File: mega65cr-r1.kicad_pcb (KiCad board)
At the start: 2 copper layers, 22 parts, among them J13 Conn_01x04_Male, J14 Conn_02x17_Odd_Even, J16 Conn_01x04_Male, J6 SDF-60J for IEC 1541 serial p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, U1 74HC245, U2 74HC245, U22 74LS06N, U3 74HC245

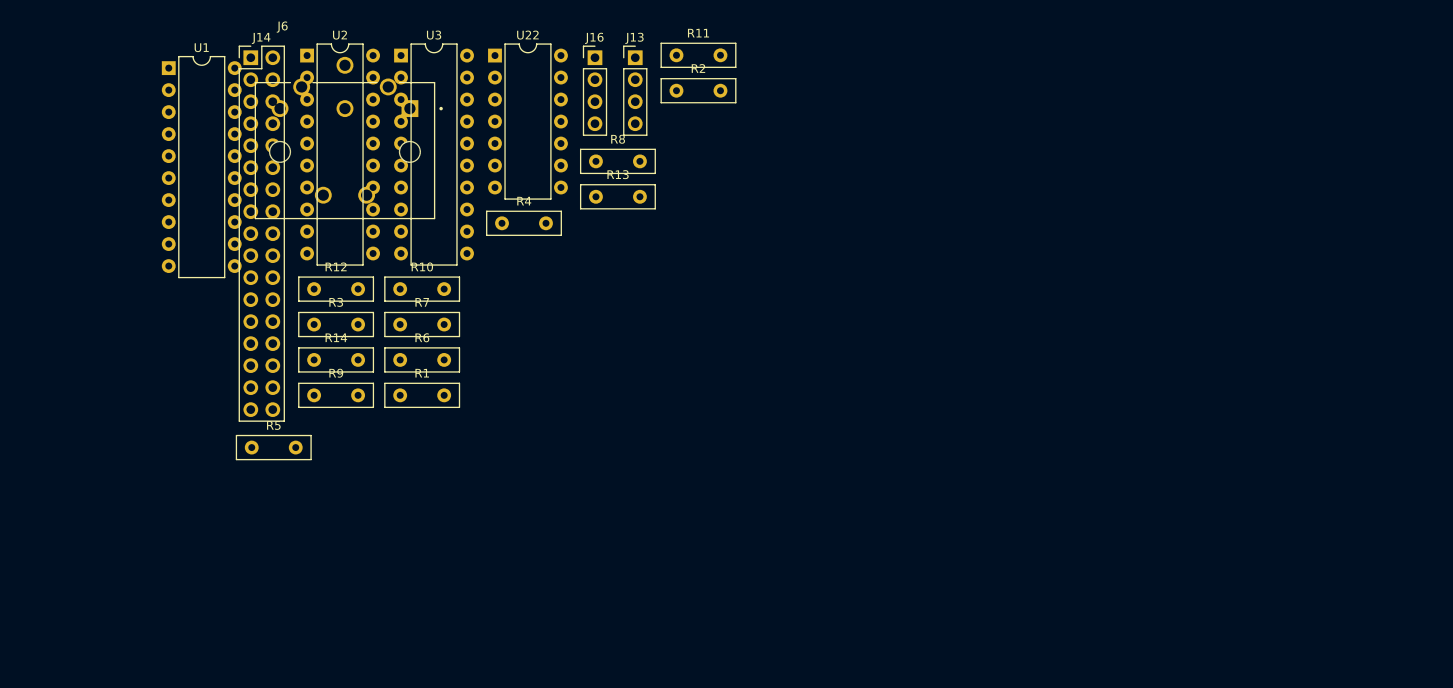
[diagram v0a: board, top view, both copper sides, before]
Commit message: add all missing footprints
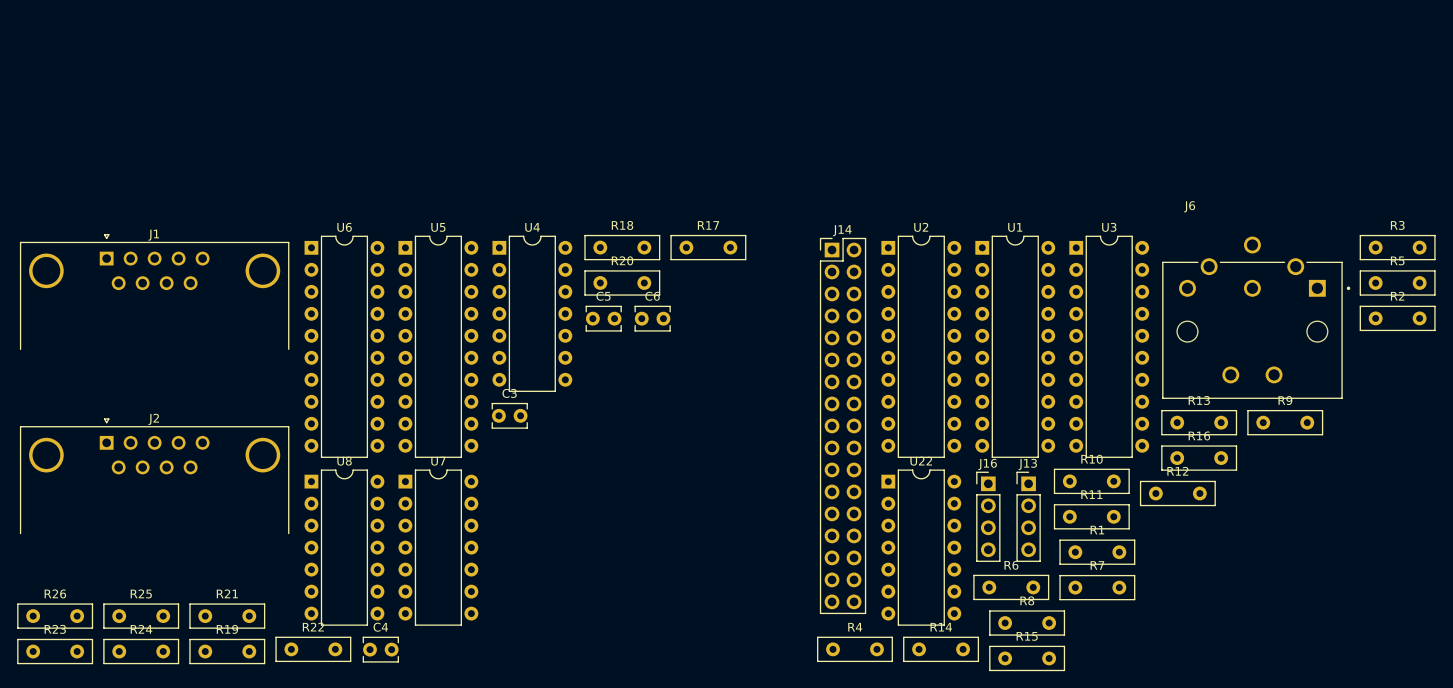
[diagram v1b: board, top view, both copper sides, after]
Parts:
- added C3: 1.2nF, Capacitor_THT:C_Disc_D3.8mm_W2.6mm_P2.50mm, F.Cu at (167.6, 124.5)
- added C4: 1.2nF, Capacitor_THT:C_Disc_D3.8mm_W2.6mm_P2.50mm, F.Cu at (152.8, 151.5)
- added C5: 1.2nF, Capacitor_THT:C_Disc_D3.8mm_W2.6mm_P2.50mm, F.Cu at (178.5, 113.2)
- added C6: 1.2nF, Capacitor_THT:C_Disc_D3.8mm_W2.6mm_P2.50mm, F.Cu at (184.1, 113.2)
- added J1: DB9_Male_MountingHoles, Connector_Dsub:DSUB-9_Male_Horizontal_P2.77x2.84mm_EdgePinOffset7.70mm_Housed_MountingHolesOffset9.12mm, F.Cu at (122.3, 106.3)
- added J2: DB9_Male_MountingHoles, Connector_Dsub:DSUB-9_Male_Horizontal_P2.77x2.84mm_EdgePinOffset7.70mm_Housed_MountingHolesOffset9.12mm, F.Cu at (122.3, 127.6)
- added R15: 4K7, Resistor_THT:R_Box_L8.4mm_W2.5mm_P5.08mm, F.Cu at (226.1, 152.5)
- added R16: 4K7, Resistor_THT:R_Box_L8.4mm_W2.5mm_P5.08mm, F.Cu at (246.0, 129.3)
- added R17: 4K7, Resistor_THT:R_Box_L8.4mm_W2.5mm_P5.08mm, F.Cu at (189.3, 105.0)
- added R18: 4K7, Resistor_THT:R_Box_L8.4mm_W2.5mm_P5.08mm, F.Cu at (179.3, 105.0)
- added R19: 4K7, Resistor_THT:R_Box_L8.4mm_W2.5mm_P5.08mm, F.Cu at (133.7, 151.7)
- added R20: 4K7, Resistor_THT:R_Box_L8.4mm_W2.5mm_P5.08mm, F.Cu at (179.3, 109.1)
- added R21: 4K7, Resistor_THT:R_Box_L8.4mm_W2.5mm_P5.08mm, F.Cu at (133.7, 147.6)
- added R22: 4K7, Resistor_THT:R_Box_L8.4mm_W2.5mm_P5.08mm, F.Cu at (143.7, 151.4)
- added R23: 4K7, Resistor_THT:R_Box_L8.4mm_W2.5mm_P5.08mm, F.Cu at (113.8, 151.7)
- added R24: 4K7, Resistor_THT:R_Box_L8.4mm_W2.5mm_P5.08mm, F.Cu at (123.8, 151.7)
- added R25: 4K7, Resistor_THT:R_Box_L8.4mm_W2.5mm_P5.08mm, F.Cu at (123.8, 147.6)
- added R26: 4K7, Resistor_THT:R_Box_L8.4mm_W2.5mm_P5.08mm, F.Cu at (113.8, 147.6)
- added U4: 74LS06N, Package_DIP:DIP-14_W7.62mm, F.Cu at (167.7, 105.1)
- added U5: 74HC245, Package_DIP:DIP-20_W7.62mm, F.Cu at (156.8, 105.1)
- added U6: 74HC245, Package_DIP:DIP-20_W7.62mm, F.Cu at (146.0, 105.1)
- added U7: 74LS06N, Package_DIP:DIP-14_W7.62mm, F.Cu at (156.8, 132.1)
- added U8: 74LS06N, Package_DIP:DIP-14_W7.62mm, F.Cu at (146.0, 132.1)
- R1, R2, R3, R4, R5: value 4K7 -> 1K
- R11, R12, R13: value 1K -> 4K7
- moved R5 131.2 mm to (268.9, 109.1)
- moved R3 122.9 mm to (268.9, 105.0)
- moved R9 109.7 mm to (255.9, 125.2)
- moved J6 106.8 mm to (254.7, 114.7)
- moved R12 100.0 mm to (243.5, 133.4)
- moved U1 96.2 mm to (223.5, 105.1)
- moved R2 84.9 mm to (268.9, 113.2)
- moved R7 83.7 mm to (234.2, 144.3)
- moved U3 81.1 mm to (234.3, 105.1)
- moved R10 80.5 mm to (233.6, 132.0)
- moved R1 80.1 mm to (234.2, 140.2)
- moved R14 77.4 mm to (216.2, 151.4)
- moved R6 72.9 mm to (224.3, 144.3)
- moved R13 72.0 mm to (246.0, 125.2)
- moved R8 71.2 mm to (226.1, 148.4)
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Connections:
- net /DIR renamed /Floppy Interfaces/DIR
- net /DRVSA renamed /Floppy Interfaces/DRVSA
- net /MOTEA renamed /Floppy Interfaces/MOTEA
- net /MOTEB renamed /Floppy Interfaces/MOTEB
- net /REDWC renamed /Floppy Interfaces/REDWC
- net /SIDE1 renamed /Floppy Interfaces/SIDE1
- net /STEP renamed /Floppy Interfaces/STEP
- net /WDATA renamed /Floppy Interfaces/WDATA
- net /WGATE renamed /Floppy Interfaces/WGATE
- J14 pad 12: /DRVSB -> /Floppy Interfaces/DRVSB
- J14 pad 26: /TRCK0 -> /Floppy Interfaces/TRCK0
- J14 pad 28: /WPROT -> /Floppy Interfaces/WPROT
- J14 pad 30: /RDATA -> /Floppy Interfaces/RDATA
- J14 pad 34: /DISKCHG -> /Floppy Interfaces/DISKCHG
- J14 pad 8: /INDEX -> /Floppy Interfaces/INDEX
- J6 pad 1: /SER_SRQ -> /Floppy Interfaces/SER_SRQ
- J6 pad 3: /SER_ATN -> /Floppy Interfaces/SER_ATN
- J6 pad 4: /SER_CLK -> /Floppy Interfaces/SER_CLK
- J6 pad 5: /SER_DATA -> /Floppy Interfaces/SER_DATA
- J6 pad 6: /SER_RESET -> /Floppy Interfaces/SER_RESET
- R1 pad 1: unconnected-(R1-Pad1) -> Net-(U2-Pad18)
- R1 pad 2: /INDEX -> /Floppy Interfaces/SER_RESET
- R10 pad 1: Net-(R10-Pad1) -> Net-(U3-Pad14)
- R10 pad 2: /DISKCHG -> /Floppy Interfaces/DISKCHG
- R11 pad 1: Net-(R11-Pad1) -> /Floppy Interfaces/DRVSB
- R11 pad 2: /SER_CLK -> +5V
- R12 pad 1: Net-(R12-Pad1) -> unconnected-(R12-Pad1)
- R12 pad 2: /SER_DATA -> /Floppy Interfaces/INDEX
- R13 pad 1: Net-(R13-Pad1) -> /Floppy Interfaces/TRCK0
- R13 pad 2: /SER_ATN -> unconnected-(R13-Pad2)
- R14 pad 1: /DRVSB -> /Floppy Interfaces/WPROT
- R14 pad 2: +5V -> unconnected-(R14-Pad2)
- R2 pad 1: /TRCK0 -> Net-(U2-Pad17)
- R2 pad 2: unconnected-(R2-Pad2) -> /Floppy Interfaces/SER_SRQ
- R3 pad 1: /WPROT -> Net-(U2-Pad16)
- R3 pad 2: unconnected-(R3-Pad2) -> /Floppy Interfaces/SER_CLK
- R4 pad 1: /RDATA -> Net-(U2-Pad15)
- R4 pad 2: unconnected-(R4-Pad2) -> /Floppy Interfaces/SER_DATA
- R5 pad 1: /DISKCHG -> Net-(U2-Pad14)
- R5 pad 2: unconnected-(R5-Pad2) -> /Floppy Interfaces/SER_ATN
- R6 pad 1: Net-(R6-Pad1) -> Net-(U3-Pad18)
- R6 pad 2: /INDEX -> /Floppy Interfaces/INDEX
- R7 pad 1: Net-(R7-Pad1) -> Net-(U3-Pad17)
- R7 pad 2: /TRCK0 -> /Floppy Interfaces/TRCK0
- R8 pad 1: Net-(R8-Pad1) -> Net-(U3-Pad16)
- R8 pad 2: /WPROT -> /Floppy Interfaces/WPROT
- R9 pad 1: Net-(R9-Pad1) -> Net-(U3-Pad15)
- R9 pad 2: /RDATA -> /Floppy Interfaces/RDATA
- U2 pad 11: Net-(R13-Pad1) -> unconnected-(U2-Pad11)
- U2 pad 12: Net-(R12-Pad1) -> unconnected-(U2-Pad12)
- U2 pad 13: Net-(R11-Pad1) -> unconnected-(U2-Pad13)
- U2 pad 14: Net-(R10-Pad1) -> Net-(U2-Pad14)
- U2 pad 15: Net-(R9-Pad1) -> Net-(U2-Pad15)
- U2 pad 16: Net-(R8-Pad1) -> Net-(U2-Pad16)
- U2 pad 17: Net-(R7-Pad1) -> Net-(U2-Pad17)
- U2 pad 18: Net-(R6-Pad1) -> Net-(U2-Pad18)
- U2 pad 2: F_INDEX -> F_SER_RESET_IN
- U2 pad 3: F_TRCK0 -> F_SER_SRQ_IN
- U2 pad 4: F_WPROT -> F_SER_CLK_IN
- U2 pad 5: F_RDATA -> F_SER_RESET_IN
- U2 pad 6: F_DISKCHG -> F_SER_ATN_IN
- U2 pad 7: F_SER_CLK_IN -> unconnected-(U2-Pad7)
- U2 pad 8: F_SER_RESET_IN -> unconnected-(U2-Pad8)
- U2 pad 9: F_SER_ATN_IN -> unconnected-(U2-Pad9)
- U22 pad 10: /SER_SRQ -> /Floppy Interfaces/SER_SRQ
- U22 pad 12: /SER_DATA -> /Floppy Interfaces/SER_DATA
- U22 pad 2: /DRVSB -> /Floppy Interfaces/DRVSB
- U22 pad 4: /SER_CLK -> /Floppy Interfaces/SER_CLK
- U22 pad 6: /SER_RESET -> /Floppy Interfaces/SER_RESET
- U22 pad 8: /SER_ATN -> /Floppy Interfaces/SER_ATN
- U3 pad 1: unconnected-(U3-Pad1) -> GND
- U3 pad 10: unconnected-(U3-Pad10) -> GND
- U3 pad 14: unconnected-(U3-Pad14) -> Net-(U3-Pad14)
- U3 pad 15: unconnected-(U3-Pad15) -> Net-(U3-Pad15)
- U3 pad 16: unconnected-(U3-Pad16) -> Net-(U3-Pad16)
- U3 pad 17: unconnected-(U3-Pad17) -> Net-(U3-Pad17)
- U3 pad 18: unconnected-(U3-Pad18) -> Net-(U3-Pad18)
- U3 pad 19: unconnected-(U3-Pad19) -> GND
- U3 pad 2: unconnected-(U3-Pad2) -> F_INDEX
- U3 pad 20: unconnected-(U3-Pad20) -> +3V3
- U3 pad 3: unconnected-(U3-Pad3) -> F_TRCK0
- U3 pad 4: unconnected-(U3-Pad4) -> F_WPROT
- U3 pad 5: unconnected-(U3-Pad5) -> F_RDATA
- U3 pad 6: unconnected-(U3-Pad6) -> F_DISKCHG

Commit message: add mezannine for joystick ports to de-clutter board.
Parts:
- added C1: 0.1uF, Capacitor_THT:C_Disc_D6.0mm_W4.4mm_P5.00mm, F.Cu at (116.8, 363.2)
- added C10: 0.1uF, Capacitor_THT:C_Disc_D6.0mm_W4.4mm_P5.00mm, F.Cu at (154.2, 333.3)
- added C11: 0.1uF, Capacitor_THT:C_Disc_D6.0mm_W4.4mm_P5.00mm, F.Cu at (131.1, 348.6)
- added C12: 15uF 50V, Capacitor_THT:CP_Radial_D5.0mm_P2.00mm, F.Cu at (351.0, 236.7)
- added C13: 15uF 50V, Capacitor_THT:CP_Radial_D5.0mm_P2.00mm, F.Cu at (382.5, 209.3)
- added C14: 15uF 50V, Capacitor_THT:CP_Radial_D5.0mm_P2.00mm, F.Cu at (339.2, 250.1)
- added C15: 0.47uF eg FG28X7R1H474KRT0, Capacitor_THT:C_Disc_D6.0mm_W4.4mm_P5.00mm, F.Cu at (368.6, 214.7)
- added C16: 100nF 50V, Capacitor_THT:C_Disc_D6.0mm_W4.4mm_P5.00mm, F.Cu at (381.7, 203.0)
- added C17: 180uF 16V, Capacitor_THT:CP_Radial_D10.0mm_P5.00mm, F.Cu at (340.4, 241.1)
- added C18: 180uF 16V, Capacitor_THT:CP_Radial_D10.0mm_P5.00mm, F.Cu at (351.9, 227.6)
- added C2: 0.01uF, eg K103Z15Y5VE5TH5, Capacitor_THT:C_Disc_D6.0mm_W4.4mm_P5.00mm, F.Cu at (125.0, 363.2)
- added C7: 0.1uF, Capacitor_THT:C_Disc_D6.0mm_W4.4mm_P5.00mm, F.Cu at (177.8, 309.8)
- added C8: 1uF, Capacitor_THT:C_Disc_D6.0mm_W4.4mm_P5.00mm, F.Cu at (131.1, 354.5)
- added C9: 10uF, Capacitor_THT:C_Disc_D6.0mm_W4.4mm_P5.00mm, F.Cu at (139.3, 347.2)
- added D1: 5V 40V 1N5825, Diode_THT:D_5KP_P12.70mm_Horizontal, F.Cu at (339.0, 216.3)
- added FB1: FerriteBead FT-3AMB4ARLY-PF, snapeda:Ferrite_Bead_Axial_L10.0mm_D4.5mm_P15.00mm_Horizontal, F.Cu at (50.9, 307.5)
- added J10: Molex 46765-2301, Connector_HDMI:HDMI_A_Contact_Technology_HDMI-19APL2_Horizontal, F.Cu at (193.0, 33.0)
- added J11: CON-SOCJ-2155, snapeda:GRAVITECH_CON-SOCJ-2155, F.Cu at (40.6, 38.1)
- added J12: Header for power lead to QMTECH WUKONG FPGA board, Connector_PinHeader_2.54mm:PinHeader_1x02_P2.54mm_Vertical, F.Cu at (362.5, 219.2)
- added J15: 696101000002 Fuse Holder 20mm, snapeda:696101000002, F.Cu at (63.5, 88.9)
- added J17: C64_Tape_Port, HackupNet:C64-Cassette-Port-Male, F.Cu at (446.5, 41.5)
- added J18: BA60BC0WT, snapeda:TO-220-FP-5, F.Cu at (138.0, 221.7)
- added J19: C64_User_Port, snapeda:C64-User-Port-Male, F.Cu at (298.3, 41.5)
- added J20: C64_Expansion_Port, HackupNet:C64-Cart-Socket-Vertical, F.Cu at (85.0, 66.0)
- added J21: Audio Header, Connector_PinHeader_2.54mm:PinHeader_1x05_P2.54mm_Vertical, F.Cu at (259.1, 245.6)
- added J22: DB15_Female_HighDensity_MountingHoles, Connector_Dsub:DSUB-15-HD_Female_Horizontal_P2.29x1.98mm_EdgePinOffset8.35mm_Housed_MountingHolesOffset10.89mm, F.Cu at (158.3, 51.5)
- added J23: 3.5mm_Stereo_Audio_Jack STX-3500-4N, Connector_Audio:Jack_3.5mm_CUI_SJ-3524-SMT_Horizontal, F.Cu at (251.5, 38.1)
- added J24: Component A/V, snapeda:CUI_SDF-80J, F.Cu at (345.4, 38.1)
- added J25: Joystick Ports Mezannine Lower, Connector_PinHeader_2.54mm:PinHeader_2x20_P2.54mm_Vertical, F.Cu at (64.8, 151.1)
- added J26: Joystick Ports Mezannine Upper, Connector_PinHeader_2.54mm:PinHeader_2x20_P2.54mm_Vertical, F.Cu at (-29.2, 163.8)
- added J3: Wuerth_7499010121A, Connector_RJ:RJ45_Wuerth_7499010121A_Horizontal, F.Cu at (210.8, 48.3)
- added J4: QMTECH FPGA Module U4, Connector_PinHeader_2.54mm:PinHeader_2x32_P2.54mm_Vertical, F.Cu at (268.0, 72.4)
- added J5: QMTECH FPGA Module U5, Connector_PinHeader_2.54mm:PinHeader_2x32_P2.54mm_Vertical, F.Cu at (268.0, 151.1)
- added J7: QMTECH JTAG, Connector_PinSocket_2.54mm:PinSocket_1x06_P2.54mm_Vertical, F.Cu at (175.2, 287.8)
- added J8: RTC, Connector_PinHeader_2.54mm:PinHeader_1x05_P2.54mm_Vertical, F.Cu at (179.8, 287.8)
- added J9: 1140084168 microSD Card Slot, snapeda:AMPHENOL_1140084168, F.Cu at (236.2, 42.2)
- added JB1: TE0790-03, Connector_PinHeader_2.54mm:PinHeader_2x06_P2.54mm_Vertical, F.Cu at (168.0, 287.8)
- added L1: 22uH, eg SC30R22KT, Inductor_THT:L_Axial_L5.0mm_D3.6mm_P10.00mm_Horizontal_Murata_BL01RN1A2A2, F.Cu at (355.5, 214.3)
- added P1: Full-side CD Card Slot, snapeda:YAMAICHI_FPS009-2405-0, F.Cu at (162.6, 154.1)
- added R11: 4K7, Resistor_THT:R_Box_L8.4mm_W2.5mm_P5.08mm, F.Cu at (38.1, 182.9)
- added R27: 220, Resistor_THT:R_Axial_DIN0204_L3.6mm_D1.6mm_P7.62mm_Horizontal, F.Cu at (167.2, 304.4)
- added R28: 220, Resistor_THT:R_Axial_DIN0204_L3.6mm_D1.6mm_P7.62mm_Horizontal, F.Cu at (183.6, 287.0)
- added R29: 6.49K 1%, Resistor_THT:R_Axial_DIN0204_L3.6mm_D1.6mm_P7.62mm_Horizontal, F.Cu at (167.2, 307.5)
- added R30: 4K7, Resistor_THT:R_Box_L8.4mm_W2.5mm_P5.08mm, F.Cu at (168.1, 314.5)
- added R31: 4K7, Resistor_THT:R_Box_L8.4mm_W2.5mm_P5.08mm, F.Cu at (184.6, 294.8)
- added R32: 4K7, Resistor_THT:R_Box_L8.4mm_W2.5mm_P5.08mm, F.Cu at (155.1, 328.3)
- added R33: 4K7, Resistor_THT:R_Box_L8.4mm_W2.5mm_P5.08mm, F.Cu at (184.6, 298.8)
- added R34: 4K7, Resistor_THT:R_Box_L8.4mm_W2.5mm_P5.08mm, F.Cu at (178.7, 304.8)
- added R35: 4K7, Resistor_THT:R_Box_L8.4mm_W2.5mm_P5.08mm, F.Cu at (145.1, 332.4)
- added R36: 12K4, Resistor_THT:R_Box_L8.4mm_W2.5mm_P5.08mm, F.Cu at (145.1, 328.3)
- added R37: 4K7, Resistor_THT:R_Box_L8.4mm_W2.5mm_P5.08mm, F.Cu at (184.6, 290.7)
- added R38: 510R, Resistor_THT:R_Box_L8.4mm_W2.5mm_P5.08mm, F.Cu at (304.4, 202.1)
- added R39: 1K0, Resistor_THT:R_Box_L8.4mm_W2.5mm_P5.08mm, F.Cu at (324.3, 210.3)
- added R40: 2K0, Resistor_THT:R_Box_L8.4mm_W2.5mm_P5.08mm, F.Cu at (302.0, 231.9)
- added R41: 4K0, Resistor_THT:R_Box_L8.4mm_W2.5mm_P5.08mm, F.Cu at (259.2, 272.3)
- added R42: 8K0, Resistor_THT:R_Box_L8.4mm_W2.5mm_P5.08mm, F.Cu at (314.3, 210.3)
- added R43: 16K0, Resistor_THT:R_Box_L8.4mm_W2.5mm_P5.08mm, F.Cu at (302.0, 227.8)
- added R44: 510R, Resistor_THT:R_Box_L8.4mm_W2.5mm_P5.08mm, F.Cu at (314.3, 218.5)
- added R45: 1K0, Resistor_THT:R_Box_L8.4mm_W2.5mm_P5.08mm, F.Cu at (314.3, 206.2)
- added R46: 2K0, Resistor_THT:R_Box_L8.4mm_W2.5mm_P5.08mm, F.Cu at (269.1, 265.7)
- added R47: 4K0, Resistor_THT:R_Box_L8.4mm_W2.5mm_P5.08mm, F.Cu at (304.4, 218.5)
- added R48: 8K0, Resistor_THT:R_Box_L8.4mm_W2.5mm_P5.08mm, F.Cu at (269.1, 257.5)
- added R49: 16K0, Resistor_THT:R_Box_L8.4mm_W2.5mm_P5.08mm, F.Cu at (324.3, 202.1)
- added R50: 510R, Resistor_THT:R_Box_L8.4mm_W2.5mm_P5.08mm, F.Cu at (263.9, 253.4)
- added R51: 1K0, Resistor_THT:R_Box_L8.4mm_W2.5mm_P5.08mm, F.Cu at (273.8, 253.4)
- added R52: 2K0, Resistor_THT:R_Box_L8.4mm_W2.5mm_P5.08mm, F.Cu at (259.2, 268.2)
- added R53: 4K0, Resistor_THT:R_Box_L8.4mm_W2.5mm_P5.08mm, F.Cu at (293.7, 240.1)
- added R54: 8K0, Resistor_THT:R_Box_L8.4mm_W2.5mm_P5.08mm, F.Cu at (302.1, 223.8)
- added R55: 16K0, Resistor_THT:R_Box_L8.4mm_W2.5mm_P5.08mm, F.Cu at (282.1, 229.1)
- added R56: 510R, Resistor_THT:R_Box_L8.4mm_W2.5mm_P5.08mm, F.Cu at (259.2, 264.2)
- added R57: 1K0, Resistor_THT:R_Box_L8.4mm_W2.5mm_P5.08mm, F.Cu at (259.2, 260.1)
- added R58: 2K0, Resistor_THT:R_Box_L8.4mm_W2.5mm_P5.08mm, F.Cu at (314.3, 202.1)
- added R59: 4K0, Resistor_THT:R_Box_L8.4mm_W2.5mm_P5.08mm, F.Cu at (292.1, 231.9)
- added R60: 8K0, Resistor_THT:R_Box_L8.4mm_W2.5mm_P5.08mm, F.Cu at (292.1, 236.0)
- added R61: 16K0, Resistor_THT:R_Box_L8.4mm_W2.5mm_P5.08mm, F.Cu at (304.4, 214.4)
- added R62: 510R, Resistor_THT:R_Box_L8.4mm_W2.5mm_P5.08mm, F.Cu at (312.0, 222.6)
- added R63: 1K0, Resistor_THT:R_Box_L8.4mm_W2.5mm_P5.08mm, F.Cu at (282.1, 225.0)
- added R64: 2K0, Resistor_THT:R_Box_L8.4mm_W2.5mm_P5.08mm, F.Cu at (263.9, 245.3)
- added R65: 4K0, Resistor_THT:R_Box_L8.4mm_W2.5mm_P5.08mm, F.Cu at (324.3, 206.2)
- added R66: 8K0, Resistor_THT:R_Box_L8.4mm_W2.5mm_P5.08mm, F.Cu at (304.4, 210.3)
- added R67: 16K0, Resistor_THT:R_Box_L8.4mm_W2.5mm_P5.08mm, F.Cu at (282.1, 237.2)
- added R68: 510R, Resistor_THT:R_Box_L8.4mm_W2.5mm_P5.08mm, F.Cu at (292.1, 227.8)
- added R69: 1K0, Resistor_THT:R_Box_L8.4mm_W2.5mm_P5.08mm, F.Cu at (269.1, 261.6)
- added R70: 2K0, Resistor_THT:R_Box_L8.4mm_W2.5mm_P5.08mm, F.Cu at (283.7, 241.3)
- added R71: 4K0, Resistor_THT:R_Box_L8.4mm_W2.5mm_P5.08mm, F.Cu at (292.1, 223.8)
- added R72: 8K0, Resistor_THT:R_Box_L8.4mm_W2.5mm_P5.08mm, F.Cu at (304.4, 206.2)
- added R73: 16K0, Resistor_THT:R_Box_L8.4mm_W2.5mm_P5.08mm, F.Cu at (314.3, 214.4)
- added R74: 510R, Resistor_THT:R_Box_L8.4mm_W2.5mm_P5.08mm, F.Cu at (283.7, 245.4)
- added R75: 1K0, Resistor_THT:R_Box_L8.4mm_W2.5mm_P5.08mm, F.Cu at (263.9, 249.4)
- added R76: 2K0, Resistor_THT:R_Box_L8.4mm_W2.5mm_P5.08mm, F.Cu at (273.8, 245.3)
- added R77: 4K0, Resistor_THT:R_Box_L8.4mm_W2.5mm_P5.08mm, F.Cu at (273.8, 249.4)
- added R78: 8K0, Resistor_THT:R_Box_L8.4mm_W2.5mm_P5.08mm, F.Cu at (283.7, 249.5)
- added R79: 16K0, Resistor_THT:R_Box_L8.4mm_W2.5mm_P5.08mm, F.Cu at (279.1, 257.5)
- added R80: 49R9, Resistor_THT:R_Box_L8.4mm_W2.5mm_P5.08mm, F.Cu at (259.2, 276.4)
- added R81: 49R9, Resistor_THT:R_Box_L8.4mm_W2.5mm_P5.08mm, F.Cu at (282.1, 233.2)
- added RN1: 3.3K x 8, Resistor_THT:R_Array_SIP9, F.Cu at (68.6, 297.2)
- added RN2: 4609X-AP1-332LF 3.3Kx8, Resistor_THT:R_Array_SIP9, F.Cu at (190.7, 269.3)
- added RN3: 3.3K x 8, Resistor_THT:R_Array_SIP9, F.Cu at (190.7, 256.2)
- added RN4: 3.3K x 8, Resistor_THT:R_Array_SIP9, F.Cu at (190.7, 260.6)
- added RN5: 3.3K x 8, Resistor_THT:R_Array_SIP9, F.Cu at (158.1, 279.9)
- added RN6: 3.3K x 8, Resistor_THT:R_Array_SIP9, F.Cu at (190.7, 264.9)
- added S1: 418117270908, snapeda:418117270908, F.Cu at (78.7, 307.3)
- added SW1: SW_Push_DPDT, snapeda:SPUJ191500, F.Cu at (17.8, 175.3)
- added U1: 74LS373, Package_DIP:DIP-20_W7.62mm, F.Cu at (257.6, 341.5)
- added U10: 74LS06N, Package_DIP:DIP-14_W7.62mm, F.Cu at (-118.1, 223.5)
- added U11: 74LS06N, Package_DIP:DIP-14_W7.62mm, F.Cu at (-41.9, 226.1)
- added U12: DP83826, Package_DFN_QFN:QFN-32-1EP_5x5mm_P0.5mm_EP3.3x3.3mm_ThermalVias, F.Cu at (210.3, 61.5)
- added U13: 74LVC374, Package_DIP:DIP-20_W7.62mm, F.Cu at (54.6, 280.7)
- added U14: PTN3363BSMP, snapeda:QFN50P500X500X85-33N, F.Cu at (193.0, 45.7)
- added U15: LM2678T-5.0, snapeda:TO127P457X1016X2052-7P, F.Cu at (346.4, 222.6)
- added U16: 74LVC374, Package_DIP:DIP-20_W7.62mm, F.Cu at (52.8, 229.0)
- added U17: 74LVC374, Package_DIP:DIP-20_W7.62mm, F.Cu at (115.6, 202.1)
- added U18: 74LS373, Package_DIP:DIP-20_W7.62mm, F.Cu at (81.1, 215.6)
- added U19: 74LS373, Package_DIP:DIP-20_W7.62mm, F.Cu at (104.7, 202.1)
- added U2: 74LVC374, Package_DIP:DIP-20_W7.62mm, F.Cu at (268.5, 287.5)
- added U20: 74LS125, Package_DIP:DIP-14_W7.62mm, F.Cu at (113.7, 229.1)
- added U21: 74LS125, Package_DIP:DIP-14_W7.62mm, F.Cu at (102.8, 229.1)
- added U23: 74LVC374, Package_DIP:DIP-20_W7.62mm, F.Cu at (126.4, 202.1)
- added U24: 74LS125, Package_DIP:DIP-14_W7.62mm, F.Cu at (124.5, 229.1)
- added U25: 74LS373, Package_DIP:DIP-20_W7.62mm, F.Cu at (63.6, 229.0)
- added U26: 74LS373, Package_DIP:DIP-20_W7.62mm, F.Cu at (92.0, 229.1)
- added U27: 74LS138, Package_DIP:DIP-16_W7.62mm, F.Cu at (203.7, 331.3)
- added U28: 74LS138, Package_DIP:DIP-16_W7.62mm, F.Cu at (214.6, 287.5)
- added U29: 74LS137, Package_DIP:DIP-16_W7.62mm, F.Cu at (203.7, 309.4)
- added U3: 74LVC374, Package_DIP:DIP-20_W7.62mm, F.Cu at (257.6, 314.5)
- added U30: 74LS137, Package_DIP:DIP-16_W7.62mm, F.Cu at (203.7, 287.5)
- added U31: 74LS04, Package_DIP:DIP-14_W7.62mm, F.Cu at (211.8, 225.8)
- added U32: 74LVC374, Package_DIP:DIP-20_W7.62mm, F.Cu at (157.5, 225.8)
- added U33: 74LVC374, Package_DIP:DIP-20_W7.62mm, F.Cu at (190.1, 229.1)
- added U34: 74LVC374, Package_DIP:DIP-20_W7.62mm, F.Cu at (200.9, 225.8)
- added U35: 74LS373, Package_DIP:DIP-20_W7.62mm, F.Cu at (240.5, 202.1)
- added U36: 74LS373, Package_DIP:DIP-20_W7.62mm, F.Cu at (179.2, 225.8)
- added U37: 74LS373, Package_DIP:DIP-20_W7.62mm, F.Cu at (168.4, 252.8)
- added U38: 74LVC374, Package_DIP:DIP-20_W7.62mm, F.Cu at (229.7, 202.1)
- added U39: 74LVC374, Package_DIP:DIP-20_W7.62mm, F.Cu at (157.5, 252.8)
- added U4: 74LS373, Package_DIP:DIP-20_W7.62mm, F.Cu at (257.6, 287.5)
- added U40: 74LS373, Package_DIP:DIP-20_W7.62mm, F.Cu at (168.4, 225.8)
- added U41: 74LS373, Package_DIP:DIP-20_W7.62mm, F.Cu at (179.2, 252.8)
- added U5: 74LS06N, Package_DIP:DIP-14_W7.62mm, F.Cu at (-123.2, 142.2)
- added U6: 74LVC374, Package_DIP:DIP-20_W7.62mm, F.Cu at (-41.9, 115.6)
- added U7: 74LVC374, Package_DIP:DIP-20_W7.62mm, F.Cu at (-156.2, 156.2)
- added U8: 74LS373, Package_DIP:DIP-20_W7.62mm, F.Cu at (-70.8, 193.0)
- added U9: 74LS373, Package_DIP:DIP-20_W7.62mm, F.Cu at (-70.8, 166.0)
- U1: value 74HC245 -> 74LS373
- U2, U3, U6: value 74HC245 -> 74LVC374
- U4, U8: value 74LS06N -> 74LS373; footprint Package_DIP:DIP-14_W7.62mm -> Package_DIP:DIP-20_W7.62mm
- U5: value 74HC245 -> 74LS06N; footprint Package_DIP:DIP-20_W7.62mm -> Package_DIP:DIP-14_W7.62mm
- U7: value 74LS06N -> 74LVC374; footprint Package_DIP:DIP-14_W7.62mm -> Package_DIP:DIP-20_W7.62mm
- moved R9 264.8 mm to (520.7, 129.5)
- moved C3 264.8 mm to (432.4, 128.8)
- moved C4 264.8 mm to (417.5, 155.8)
- moved C6 264.8 mm to (448.9, 117.5)
- moved J13 264.8 mm to (493.6, 136.6)
- moved R10 264.8 mm to (498.4, 136.3)
- moved R11 264.8 mm to (498.4, 140.4)
- moved R12 264.8 mm to (508.3, 137.7)
- moved U3 264.8 mm to (499.1, 109.3)
- moved U4 264.8 mm to (432.5, 109.3)
- moved C5 264.8 mm to (443.3, 117.5)
- moved J14 264.8 mm to (470.9, 109.6)
- moved J16 264.8 mm to (488.9, 136.6)
- moved R1 264.8 mm to (499.0, 144.5)
- moved R13 264.8 mm to (510.8, 129.5)
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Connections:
- net /Floppy Interfaces/MOTEB renamed /IEC & 3.5" Drives/MOTEB
- net F_SER_SRQ_OUT renamed /IEC & 3.5" Drives/SER_SRQ_OUT
- J14 pad 10: /Floppy Interfaces/MOTEA -> /IEC & 3.5" Drives/MOTEA
- J14 pad 12: /Floppy Interfaces/DRVSB -> /IEC & 3.5" Drives/DRVSB
- J14 pad 14: /Floppy Interfaces/DRVSA -> /IEC & 3.5" Drives/DRVSA
- J14 pad 18: /Floppy Interfaces/DIR -> /IEC & 3.5" Drives/DIR
- J14 pad 2: /Floppy Interfaces/REDWC -> /IEC & 3.5" Drives/REDWC
- J14 pad 20: /Floppy Interfaces/STEP -> /IEC & 3.5" Drives/STEP
- J14 pad 22: /Floppy Interfaces/WDATA -> /IEC & 3.5" Drives/WDATA
- J14 pad 24: /Floppy Interfaces/WGATE -> /IEC & 3.5" Drives/WGATE
- J14 pad 26: /Floppy Interfaces/TRCK0 -> /IEC & 3.5" Drives/TRCK0
- J14 pad 28: /Floppy Interfaces/WPROT -> /IEC & 3.5" Drives/WPROT
- J14 pad 30: /Floppy Interfaces/RDATA -> /IEC & 3.5" Drives/RDATA
- J14 pad 32: /Floppy Interfaces/SIDE1 -> /IEC & 3.5" Drives/SIDE1
- J14 pad 34: /Floppy Interfaces/DISKCHG -> /IEC & 3.5" Drives/DISKCHG
- J14 pad 8: /Floppy Interfaces/INDEX -> /IEC & 3.5" Drives/INDEX
- J6 pad 1: /Floppy Interfaces/SER_SRQ -> /IEC & 3.5" Drives/SER_SRQ
- J6 pad 3: /Floppy Interfaces/SER_ATN -> IEC_ATN
- J6 pad 4: /Floppy Interfaces/SER_CLK -> /IEC & 3.5" Drives/SER_CLK
- J6 pad 5: /Floppy Interfaces/SER_DATA -> /IEC & 3.5" Drives/SER_DATA
- J6 pad 6: /Floppy Interfaces/SER_RESET -> /IEC & 3.5" Drives/SER_RESET
- R1 pad 1: Net-(U2-Pad18) -> /IEC & 3.5" Drives/SER_RESET
- R1 pad 2: /Floppy Interfaces/SER_RESET -> Net-(R1-Pad2)
- R10 pad 1: Net-(U3-Pad14) -> /IEC & 3.5" Drives/DISKCHG
- R10 pad 2: /Floppy Interfaces/DISKCHG -> Net-(R10-Pad2)
- R11 pad 1: /Floppy Interfaces/DRVSB -> /Joystick Ports/RESET_BTN
- R12 pad 2: /Floppy Interfaces/INDEX -> /IEC & 3.5" Drives/INDEX
- R13 pad 1: /Floppy Interfaces/TRCK0 -> /IEC & 3.5" Drives/TRCK0
- R14 pad 1: /Floppy Interfaces/WPROT -> /IEC & 3.5" Drives/WPROT
- R15 pad 1: /Floppy Interfaces/DISKCHG -> /IEC & 3.5" Drives/DISKCHG
- R16 pad 1: /Floppy Interfaces/RDATA -> /IEC & 3.5" Drives/RDATA
- R2 pad 1: Net-(U2-Pad17) -> /IEC & 3.5" Drives/SER_SRQ
- R2 pad 2: /Floppy Interfaces/SER_SRQ -> Net-(R2-Pad2)
- R3 pad 1: Net-(U2-Pad16) -> /IEC & 3.5" Drives/SER_CLK
- R3 pad 2: /Floppy Interfaces/SER_CLK -> Net-(R3-Pad2)
- R4 pad 1: Net-(U2-Pad15) -> /IEC & 3.5" Drives/SER_DATA
- R4 pad 2: /Floppy Interfaces/SER_DATA -> Net-(R4-Pad2)
- R5 pad 1: Net-(U2-Pad14) -> IEC_ATN
- R5 pad 2: /Floppy Interfaces/SER_ATN -> Net-(R5-Pad2)
- R6 pad 1: Net-(U3-Pad18) -> /IEC & 3.5" Drives/INDEX
- R6 pad 2: /Floppy Interfaces/INDEX -> Net-(R6-Pad2)
- R7 pad 1: Net-(U3-Pad17) -> /IEC & 3.5" Drives/TRCK0
- R7 pad 2: /Floppy Interfaces/TRCK0 -> Net-(R7-Pad2)
- R8 pad 1: Net-(U3-Pad16) -> /IEC & 3.5" Drives/WPROT
- R8 pad 2: /Floppy Interfaces/WPROT -> Net-(R8-Pad2)
- R9 pad 1: Net-(U3-Pad15) -> /IEC & 3.5" Drives/RDATA
- R9 pad 2: /Floppy Interfaces/RDATA -> Net-(R9-Pad2)
- U1 pad 1: +5V -> GND
- U1 pad 11: /Floppy Interfaces/SIDE1 -> MUX_LATCH_0
- U1 pad 12: /Floppy Interfaces/WGATE -> /IEC & 3.5" Drives/STEP
- U1 pad 13: /Floppy Interfaces/WDATA -> MUX_DO4
- U1 pad 14: /Floppy Interfaces/STEP -> MUX_DO5
- U1 pad 15: /Floppy Interfaces/DIR -> /IEC & 3.5" Drives/WDATA
- U1 pad 16: /Floppy Interfaces/DRVSA -> /IEC & 3.5" Drives/WGATE
- U1 pad 17: /Floppy Interfaces/MOTEA -> MUX_DO6
- U1 pad 18: /Floppy Interfaces/REDWC -> MUX_DO7
- U1 pad 19: GND -> /IEC & 3.5" Drives/SIDE1
- U1 pad 2: F_REDWC -> /IEC & 3.5" Drives/REDWC
- U1 pad 3: F_MOTEA -> MUX_DO0
- U1 pad 4: F_DRVSA -> MUX_DO1
- U1 pad 5: F_DIR -> /IEC & 3.5" Drives/MOTEA
- U1 pad 6: F_STEP -> /IEC & 3.5" Drives/DRVSA
- U1 pad 7: F_WDATA -> MUX_DO2
- U1 pad 8: F_WGATE -> MUX_DO3
- U1 pad 9: F_SIDE1 -> /IEC & 3.5" Drives/DIR
- U2 pad 1: GND -> MUX_LATCH_0_N
- U2 pad 11: unconnected-(U2-Pad11) -> MUX_LATCH_0
- U2 pad 12: unconnected-(U2-Pad12) -> MUX_DI4
- U2 pad 13: unconnected-(U2-Pad13) -> Net-(R10-Pad2)
- U2 pad 14: Net-(U2-Pad14) -> unconnected-(U2-Pad14)
- U2 pad 15: Net-(U2-Pad15) -> unconnected-(U2-Pad15)
- U2 pad 16: Net-(U2-Pad16) -> unconnected-(U2-Pad16)
- U2 pad 17: Net-(U2-Pad17) -> unconnected-(U2-Pad17)
- U2 pad 18: Net-(U2-Pad18) -> unconnected-(U2-Pad18)
- U2 pad 19: GND -> unconnected-(U2-Pad19)
- U2 pad 2: F_SER_RESET_IN -> MUX_DI0
- U2 pad 3: F_SER_SRQ_IN -> Net-(R6-Pad2)
- U2 pad 4: F_SER_CLK_IN -> Net-(R7-Pad2)
- U2 pad 5: F_SER_RESET_IN -> MUX_DI1
- U2 pad 6: F_SER_ATN_IN -> MUX_DI2
- U2 pad 7: unconnected-(U2-Pad7) -> Net-(R8-Pad2)
- U2 pad 8: unconnected-(U2-Pad8) -> Net-(R9-Pad2)
- U2 pad 9: unconnected-(U2-Pad9) -> MUX_DI3
- U22 pad 1: F_DRVSB -> GND
- U22 pad 10: /Floppy Interfaces/SER_SRQ -> /IEC & 3.5" Drives/SER_SRQ
- U22 pad 12: /Floppy Interfaces/SER_DATA -> /IEC & 3.5" Drives/SER_DATA
- U22 pad 13: F_SER_DATA_OUT -> /IEC & 3.5" Drives/SER_DATA_OUT
- U22 pad 2: /Floppy Interfaces/DRVSB -> unconnected-(U22-Pad2)
- U22 pad 3: F_SER_CLK_OUT -> /IEC & 3.5" Drives/SER_CLK_OUT
- U22 pad 4: /Floppy Interfaces/SER_CLK -> /IEC & 3.5" Drives/SER_CLK
- U22 pad 5: F_SER_RESET_OUT -> /IEC & 3.5" Drives/SER_RESET_OUT
- U22 pad 6: /Floppy Interfaces/SER_RESET -> /IEC & 3.5" Drives/SER_RESET
- U22 pad 8: /Floppy Interfaces/SER_ATN -> IEC_ATN
- U22 pad 9: F_SER_ATN_OUT -> /IEC & 3.5" Drives/SER_ATN_OUT
- U3 pad 1: GND -> MUX_LATCH_1_N
- U3 pad 11: unconnected-(U3-Pad11) -> MUX_LATCH_1
- U3 pad 12: unconnected-(U3-Pad12) -> MUX_DI4
- U3 pad 13: unconnected-(U3-Pad13) -> Net-(R5-Pad2)
- U3 pad 14: Net-(U3-Pad14) -> unconnected-(U3-Pad14)
- U3 pad 15: Net-(U3-Pad15) -> unconnected-(U3-Pad15)
- U3 pad 16: Net-(U3-Pad16) -> unconnected-(U3-Pad16)
- U3 pad 17: Net-(U3-Pad17) -> unconnected-(U3-Pad17)
- U3 pad 18: Net-(U3-Pad18) -> unconnected-(U3-Pad18)
- U3 pad 19: GND -> unconnected-(U3-Pad19)
- U3 pad 2: F_INDEX -> MUX_DI0
- U3 pad 3: F_TRCK0 -> Net-(R1-Pad2)
- U3 pad 4: F_WPROT -> Net-(R2-Pad2)
- U3 pad 5: F_RDATA -> MUX_DI1
- U3 pad 6: F_DISKCHG -> MUX_DI2
- U3 pad 7: unconnected-(U3-Pad7) -> Net-(R3-Pad2)
- U3 pad 8: unconnected-(U3-Pad8) -> Net-(R4-Pad2)
- U3 pad 9: unconnected-(U3-Pad9) -> MUX_DI3
- U4 pad 1: unconnected-(U4-Pad1) -> GND
- U4 pad 10: unconnected-(U4-Pad10) -> GND
- U4 pad 11: unconnected-(U4-Pad11) -> MUX_LATCH_1
- U4 pad 12: unconnected-(U4-Pad12) -> /IEC & 3.5" Drives/SER_ATN_OUT
- U4 pad 13: unconnected-(U4-Pad13) -> MUX_DO4
- U4 pad 14: +5V -> MUX_DO5
- U4 pad 2: /Joystick Ports/JA_AY -> /IEC & 3.5" Drives/SER_RESET_OUT
- U4 pad 3: F_JB_AY_OUT -> MUX_DO0
- U4 pad 4: /Joystick Ports/JB_AY -> MUX_DO1
- U4 pad 5: unconnected-(U4-Pad5) -> /IEC & 3.5" Drives/SER_SEQ_OUT
- U4 pad 6: unconnected-(U4-Pad6) -> /IEC & 3.5" Drives/SER_CLK_OUT
- U4 pad 7: GND -> MUX_DO2
- U4 pad 8: unconnected-(U4-Pad8) -> MUX_DO3
- U4 pad 9: unconnected-(U4-Pad9) -> /IEC & 3.5" Drives/SER_DATA_OUT
- U5 pad 1: +5V -> Net-(U5-Pad1)
- U5 pad 10: GND -> unconnected-(U5-Pad10)
- U5 pad 11: unconnected-(U5-Pad11) -> /Joystick Ports/M_GND
- U5 pad 12: F_JA_UP_IN -> unconnected-(U5-Pad12)
- U5 pad 13: F_JA_FIRE_IN -> /Joystick Ports/M_GND
- U5 pad 14: F_JA_DOWN_IN -> /Joystick Ports/M_5V
- U5 pad 2: /Joystick Ports/JA_AY -> /Joystick Ports/M_JA_AY
- U5 pad 3: /Joystick Ports/JA_AX -> Net-(U5-Pad3)
- U5 pad 4: /Joystick Ports/JA_RIGHT -> /Joystick Ports/M_JA_AX
- U5 pad 5: /Joystick Ports/JA_LEFT -> /Joystick Ports/M_GND
- U5 pad 6: /Joystick Ports/JA_DOWN -> unconnected-(U5-Pad6)
- U5 pad 7: /Joystick Ports/JA_FIRE -> /Joystick Ports/M_GND
- U5 pad 8: /Joystick Ports/JA_UP -> unconnected-(U5-Pad8)
- U5 pad 9: unconnected-(U5-Pad9) -> /Joystick Ports/M_GND
- U6 pad 1: +5V -> /Joystick Ports/M_MUX_SEL_2_N
- U6 pad 10: GND -> /Joystick Ports/M_GND
- U6 pad 11: unconnected-(U6-Pad11) -> /Joystick Ports/M_MUX_SEL_2
- U6 pad 12: F_JB_UP_IN -> /Joystick Ports/M_MUX_DI4
- U6 pad 13: F_JB_FIRE_IN -> /Joystick Ports/M_JA_DOWN
- U6 pad 14: F_JB_DOWN_IN -> /Joystick Ports/M_JA_FIRE
- U6 pad 15: F_JB_LEFT_IN -> /Joystick Ports/M_MUX_DI5
- U6 pad 16: F_JB_RIGHT_IN -> /Joystick Ports/M_MUX_DI6
- U6 pad 17: F_JB_AY_IN -> /Joystick Ports/M_JA_UP
- U6 pad 18: F_JB_AX_IN -> /Joystick Ports/M_RESET_BTN
- U6 pad 19: GND -> /Joystick Ports/M_MUX_DI7
- U6 pad 2: /Joystick Ports/JB_AY -> /Joystick Ports/M_MUX_DI0
- U6 pad 20: +3V3 -> /Joystick Ports/M_3V3
- U6 pad 3: /Joystick Ports/JB_AX -> /Joystick Ports/M_JA_AY
- U6 pad 4: /Joystick Ports/JB_RIGHT -> /Joystick Ports/M_JA_AX
- U6 pad 5: /Joystick Ports/JB_LEFT -> /Joystick Ports/M_MUX_DI1
- U6 pad 6: /Joystick Ports/JB_DOWN -> /Joystick Ports/M_MUX_DI2
- U6 pad 7: /Joystick Ports/JB_FIRE -> /Joystick Ports/M_JA_RIGHT
- U6 pad 8: /Joystick Ports/JB_UP -> /Joystick Ports/M_JA_LEFT
- U6 pad 9: unconnected-(U6-Pad9) -> /Joystick Ports/M_M_MUX_DI3
- U7 pad 1: F_JA_RIGHT_OUT -> /Joystick Ports/M_MUX_SEL_3_N
- U7 pad 10: /Joystick Ports/JB_FIRE -> /Joystick Ports/M_GND
- U7 pad 11: F_JB_FIRE_OUT -> /Joystick Ports/M_MUX_SEL_3
- U7 pad 12: /Joystick Ports/JB_AX -> /Joystick Ports/M_MUX_DI4
- U7 pad 13: F_JB_AX_OUT -> /Joystick Ports/M_JB_DOWN
- U7 pad 14: +5V -> /Joystick Ports/M_JB_FIRE
- U7 pad 2: /Joystick Ports/JA_RIGHT -> /Joystick Ports/M_MUX_DI0
- U7 pad 3: F_JA_LEFT_OUT -> /Joystick Ports/M_JB_AY
- U7 pad 4: /Joystick Ports/JA_LEFT -> /Joystick Ports/M_JB_AX
- U7 pad 5: F_JA_DOWN_OUT -> /Joystick Ports/M_MUX_DI1
- U7 pad 6: /Joystick Ports/JA_DOWN -> /Joystick Ports/M_MUX_DI2
- U7 pad 7: GND -> /Joystick Ports/M_JB_RIGHT
- U7 pad 8: /Joystick Ports/JA_UP -> /Joystick Ports/M_JB_LEFT
- U7 pad 9: F_JA_UP_OUT -> /Joystick Ports/M_MUX_DI3
- U8 pad 1: F_JB_RIGHT_OUT -> /Joystick Ports/M_GND
- U8 pad 10: /Joystick Ports/JA_FIRE -> /Joystick Ports/M_GND
- U8 pad 11: F_JA_FIRE_OUT -> /Joystick Ports/M_MUX_SEL_2
- U8 pad 12: /Joystick Ports/JA_AX -> Net-(U10-Pad11)
- U8 pad 13: F_JA_AX_OUT -> /Joystick Ports/M_MUX_DO4
- U8 pad 14: +5V -> /Joystick Ports/M_MUX_DO5
- U8 pad 2: /Joystick Ports/JB_RIGHT -> Net-(U5-Pad1)
- U8 pad 3: F_JB_LEFT_OUT -> /Joystick Ports/M_MUX_DO0
- U8 pad 4: /Joystick Ports/JB_LEFT -> /Joystick Ports/M_MUX_DO1
- U8 pad 5: F_JB_DOWN_OUT -> Net-(U5-Pad3)
- U8 pad 6: /Joystick Ports/JB_DOWN -> Net-(U10-Pad5)
- U8 pad 7: GND -> /Joystick Ports/M_MUX_DO2
- U8 pad 8: /Joystick Ports/JB_UP -> /Joystick Ports/M_MUX_DO3
- U8 pad 9: F_JB_UP_OUT -> Net-(U10-Pad9)
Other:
- board outline added: 435 x 140 mm

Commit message: start routing joystick mezzannine
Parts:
- removed the U5 at (-90.2, 50.8)
- removed the U6 at (-64.8, 87.6)
- removed the U7 at (-69.8, 265.4)
- removed the U8 at (-113.0, 105.4)
- moved U7 585.9 mm to (423.0, 68.5)
- moved U10 580.5 mm to (447.2, 91.4)
- moved U5 575.1 mm to (447.2, 68.6)
- moved U8 524.1 mm to (447.2, 113.0)
- moved U9 510.9 mm to (435.6, 98.6)
- moved J26 493.7 mm to (458.6, 87.6)
- moved U11 482.0 mm to (423.0, 99.1)
- moved U6 479.9 mm to (435.7, 68.6)
- moved J13 251.1 mm to (384.4, 362.7)
- moved R11 251.1 mm to (389.1, 366.5)
- moved R9 251.1 mm to (411.5, 355.6)
- moved U1 251.1 mm to (379.0, 335.4)
- moved U3 251.1 mm to (389.9, 335.4)
- moved U4 251.1 mm to (323.3, 335.4)
- moved C3 251.1 mm to (323.2, 354.8)
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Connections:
- J25 pad 13: /Joystick Ports/JA_DOWN -> /Joystick Ports/JA_RIGHT
- J25 pad 15: /Joystick Ports/JA_FIRE -> /Joystick Ports/JA_AX
- J25 pad 17: /Joystick Ports/JA_UP -> /Joystick Ports/JA_AY
- J25 pad 21: /Joystick Ports/JB_AY -> /Joystick Ports/JB_UP
- J25 pad 23: /Joystick Ports/JB_AX -> /Joystick Ports/JB_FIRE
- J25 pad 25: /Joystick Ports/JB_RIGHT -> /Joystick Ports/JB_DOWN
- J25 pad 29: /Joystick Ports/JB_DOWN -> /Joystick Ports/JB_RIGHT
- J25 pad 31: /Joystick Ports/JB_FIRE -> /Joystick Ports/JB_AX
- J25 pad 33: /Joystick Ports/JB_UP -> /Joystick Ports/JB_AY
- J25 pad 5: /Joystick Ports/JA_AY -> /Joystick Ports/JA_UP
- J25 pad 7: /Joystick Ports/JA_AX -> /Joystick Ports/JA_FIRE
- J25 pad 9: /Joystick Ports/JA_RIGHT -> /Joystick Ports/JA_DOWN
- J26 pad 1: /Joystick Ports/M_5V -> +5V
- J26 pad 13: /Joystick Ports/M_JA_DOWN -> /Joystick Ports/M_JA_RIGHT
- J26 pad 15: /Joystick Ports/M_JA_FIRE -> /Joystick Ports/M_JA_AX
- J26 pad 17: /Joystick Ports/M_JA_UP -> /Joystick Ports/M_JA_AY
- J26 pad 2: /Joystick Ports/M_3V3 -> +3V3
- J26 pad 21: /Joystick Ports/M_JB_AY -> /Joystick Ports/M_JB_UP
- J26 pad 23: /Joystick Ports/M_JB_AX -> /Joystick Ports/M_JB_FIRE
- J26 pad 25: /Joystick Ports/M_JB_RIGHT -> /Joystick Ports/M_JB_DOWN
- J26 pad 29: /Joystick Ports/M_JB_DOWN -> /Joystick Ports/M_JB_RIGHT
- J26 pad 3: /Joystick Ports/M_GND -> GND
- J26 pad 31: /Joystick Ports/M_JB_FIRE -> /Joystick Ports/M_JB_AX
- J26 pad 33: /Joystick Ports/M_JB_UP -> /Joystick Ports/M_JB_AY
- J26 pad 4: /Joystick Ports/M_GND -> GND
- J26 pad 5: /Joystick Ports/M_JA_AY -> /Joystick Ports/M_JA_UP
- J26 pad 7: /Joystick Ports/M_JA_AX -> /Joystick Ports/M_JA_FIRE
- J26 pad 9: /Joystick Ports/M_JA_RIGHT -> /Joystick Ports/M_JA_DOWN
- U10 pad 14: /Joystick Ports/M_5V -> +5V
- U10 pad 7: /Joystick Ports/M_GND -> GND
- U11 pad 14: /Joystick Ports/M_5V -> +5V
- U11 pad 7: /Joystick Ports/M_GND -> GND
- U5 pad 11: /Joystick Ports/M_GND -> GND
- U5 pad 13: /Joystick Ports/M_GND -> GND
- U5 pad 14: /Joystick Ports/M_5V -> +5V
- U5 pad 5: /Joystick Ports/M_GND -> GND
- U5 pad 7: /Joystick Ports/M_GND -> GND
- U5 pad 9: /Joystick Ports/M_GND -> GND
- U6 pad 10: /Joystick Ports/M_GND -> GND
- U6 pad 20: /Joystick Ports/M_3V3 -> +3V3
- U7 pad 10: /Joystick Ports/M_GND -> GND
- U7 pad 20: /Joystick Ports/M_3V3 -> +3V3
- U8 pad 1: /Joystick Ports/M_GND -> GND
- U8 pad 10: /Joystick Ports/M_GND -> GND
- U8 pad 13: /Joystick Ports/M_MUX_DO4 -> /Joystick Ports/M_MUX_DO5
- U8 pad 14: /Joystick Ports/M_MUX_DO5 -> /Joystick Ports/M_MUX_DO4
- U8 pad 20: /Joystick Ports/M_5V -> +5V
- U9 pad 1: /Joystick Ports/M_GND -> GND
- U9 pad 10: /Joystick Ports/M_GND -> GND
- U9 pad 20: /Joystick Ports/M_5V -> +5V
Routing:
- net +5V: track 0.00 -> 104.3 mm
- net /Joystick Ports/M_MUX_SEL_3_N: track 0.00 -> 93.6 mm
- net /Joystick Ports/M_JB_RIGHT: track 0.00 -> 57.9 mm
- net /Joystick Ports/M_JB_UP: track 0.00 -> 45.0 mm
- net /Joystick Ports/M_MUX_DO2: track 0.00 -> 37.4 mm
- net /Joystick Ports/M_MUX_DO3: track 0.00 -> 37.4 mm
- net +3V3: track 0.00 -> 34.7 mm
- net /Joystick Ports/M_MUX_SEL_3: track 0.00 -> 22.9 mm
- net Net-(U11-Pad3): track 0.00 -> 22.3 mm
- net Net-(U11-Pad11): track 0.00 -> 18.6 mm
- net /Joystick Ports/M_MUX_DO0: track 0.00 -> 16.1 mm
- net /Joystick Ports/M_MUX_DO1: track 0.00 -> 16.1 mm
- net /Joystick Ports/M_MUX_DI0: track 0.00 -> 13.7 mm
- net /Joystick Ports/M_MUX_DI4: track 0.00 -> 13.6 mm
- net /Joystick Ports/M_MUX_DI6: track 0.00 -> 13.6 mm
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- added copper zone on In1.Cu, net GND
- added copper zone on In2.Cu, net GND
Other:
- outline, holes or cut-outs redrawn
- copper layers 2 -> 4
- board text added: "MEGA65CR R1 Joystick Port Mezzannine"
